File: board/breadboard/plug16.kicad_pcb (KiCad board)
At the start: 2 copper layers, 34 x 19.1 mm, 3 parts, among them J1 Conn_01x12, J2 Moat_Bus_wire, J3 Conn_01x12

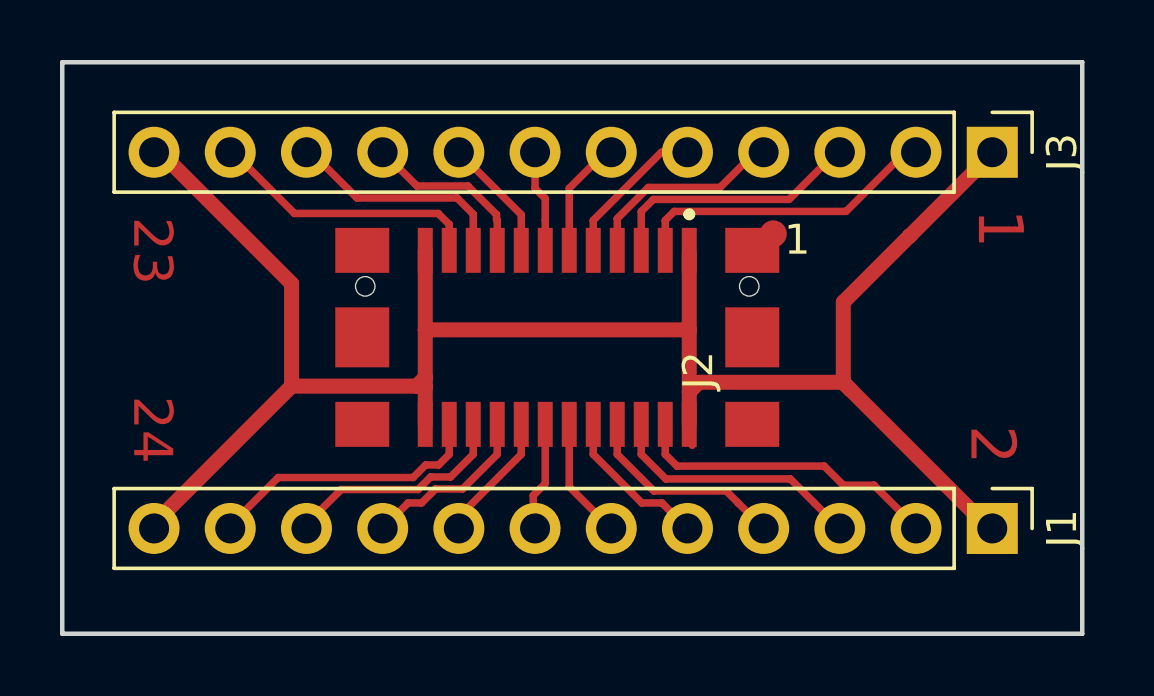
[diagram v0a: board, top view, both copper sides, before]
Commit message: Too many reworks to count.
Most notably: Split GND and GNDPWR.
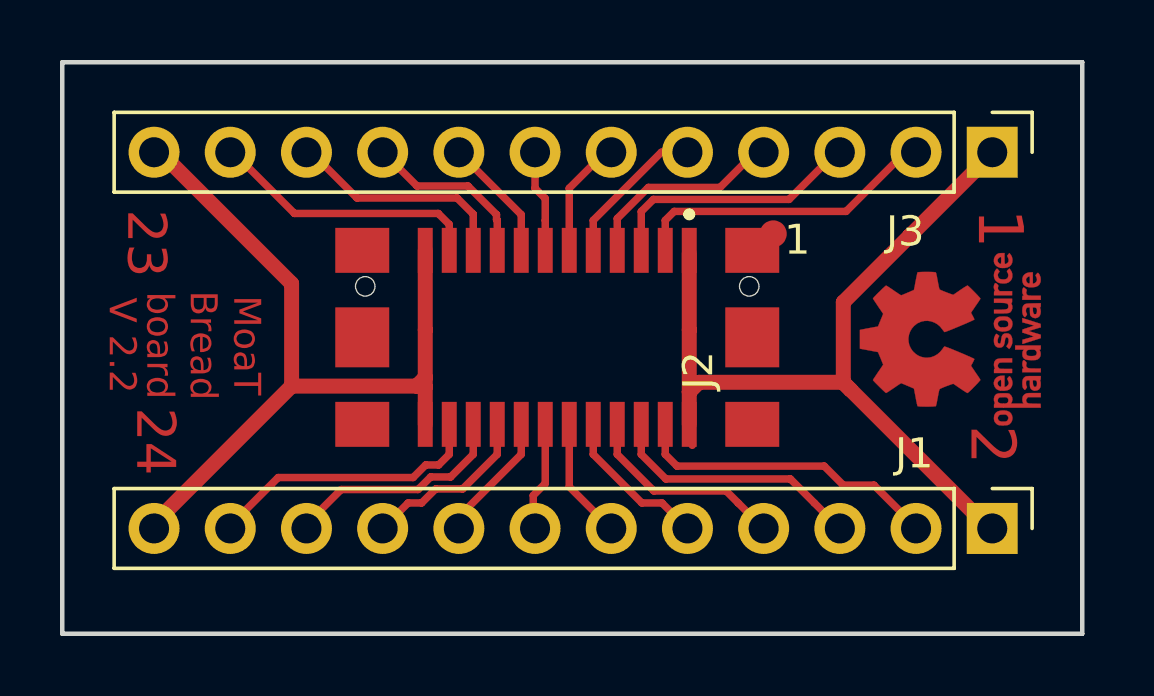
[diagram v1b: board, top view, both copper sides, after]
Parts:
- added REF**: OSHW-Logo_5.7x6mm_Copper, Symbol:OSHW-Logo_5.7x6mm_Copper, F.Cu at (29.6, 6.70)
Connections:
- J1 pad 12: GND -> GNDPWR
- J2 pad 23: GND -> GNDPWR
- J2 pad 24: GND -> GNDPWR
- J3 pad 12: GND -> GNDPWR
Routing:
- net GND: track 64.4 -> 28.8 mm
- net GNDPWR: track 0.00 -> 26.9 mm
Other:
- board text added: "MoaT Bread board"
- board text added: "V 2.2"
